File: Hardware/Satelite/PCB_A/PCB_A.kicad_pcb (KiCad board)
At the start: 2 copper layers, 54 x 54 mm, 82 parts, among them J1 Batería LiPo (Soldada), J2 CONUFL001-SMD, J3 Servo Globo, J4 Conector_PCB_A-B, J5 Servo Paracaídas, M1 Spacer, M2 Spacer, M3 Spacer, Q1 SSM3J338R,LF, Q2 BC817, U1 A2235-H, U2 CC1101RGP, U3 0915BM15A0001E, U4 AP9211SA-AF-HAC-7, U5 B39921B3588U410, U6 CC1190, Y1 26 MHz

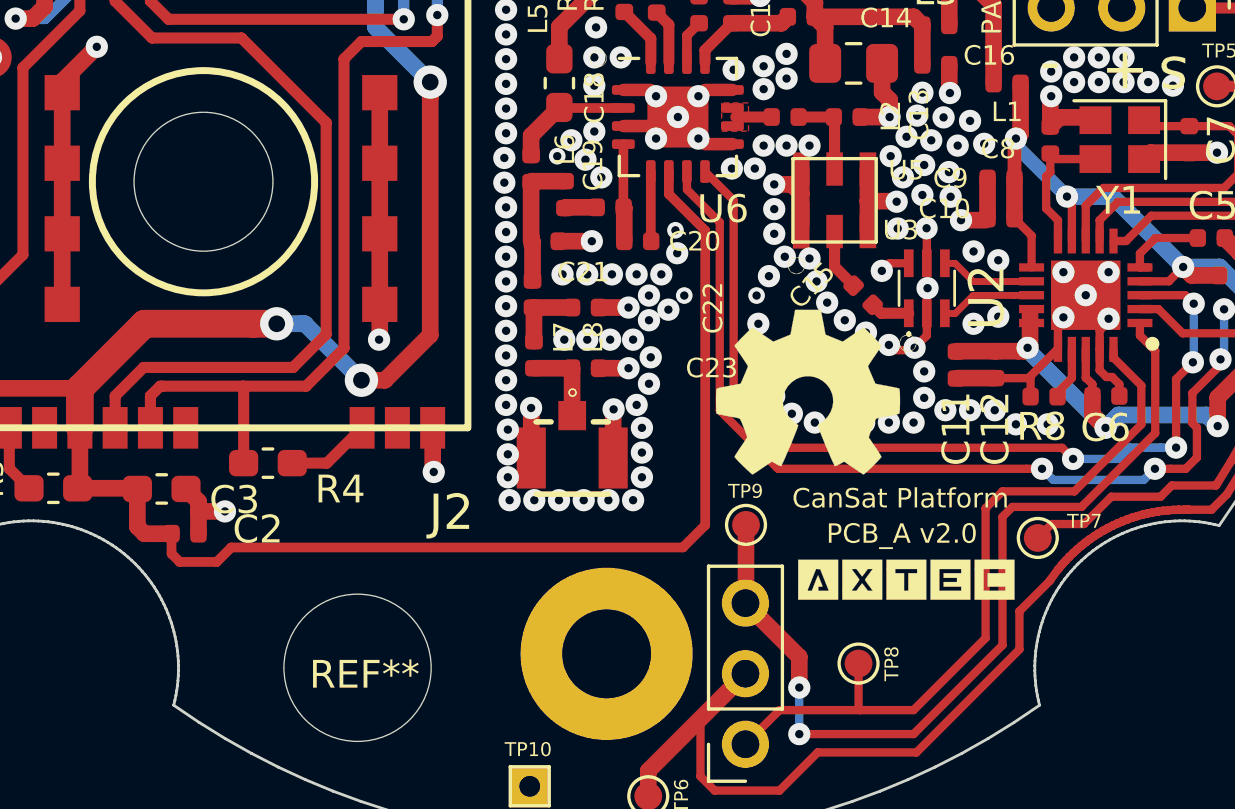
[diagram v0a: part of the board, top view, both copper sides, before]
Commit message: Agregado jumper de seleción de ganacia para CC1190 en ET
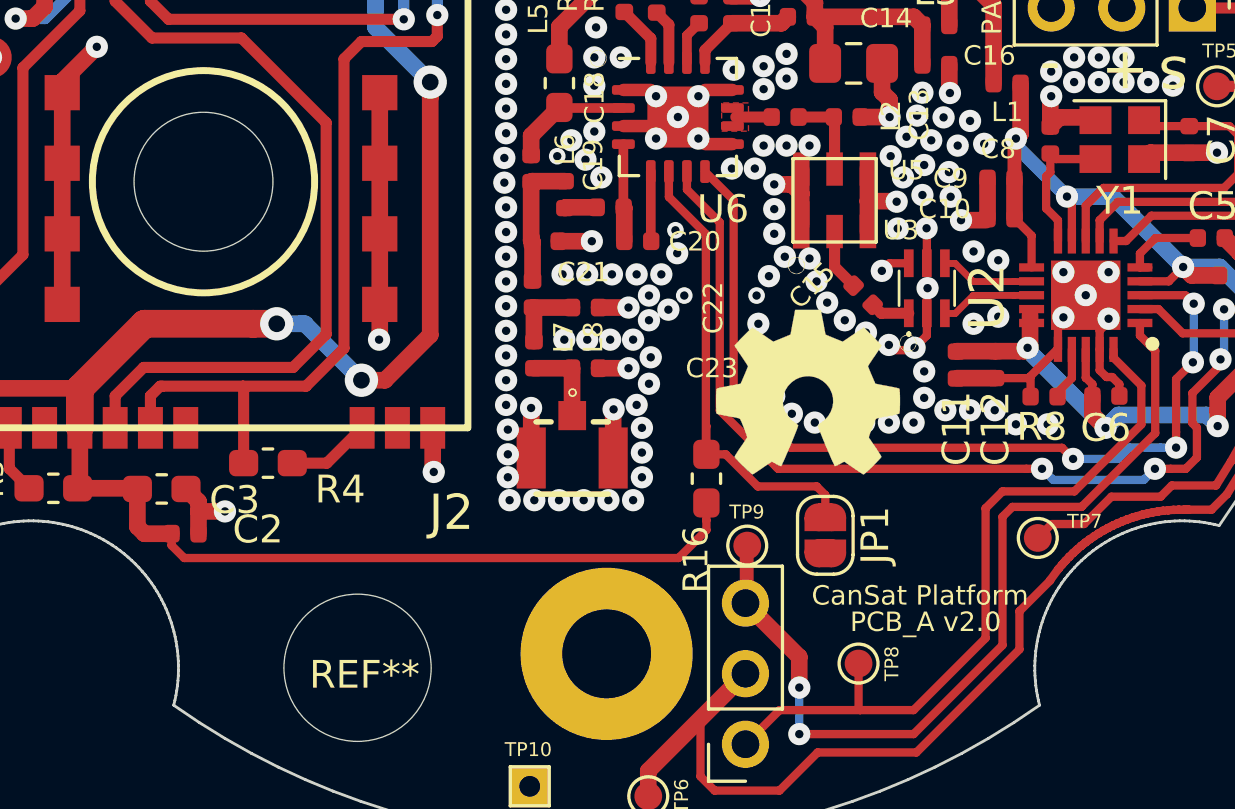
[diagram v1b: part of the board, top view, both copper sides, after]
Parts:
- removed G*** (x2): LOGO, AXTEC:Logo_AXTEC
- added JP1: Jumper, Jumper:SolderJumper-2_P1.3mm_Open_RoundedPad1.0x1.5mm, F.Cu at (7.87, 15.9)
- added R16: 10K, Resistor_SMD:R_0603_1608Metric_Pad1.05x0.95mm_HandSolder, F.Cu at (3.59, 13.9)
- moved TP9 0.75 mm to (5.06, 16.3)
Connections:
- S1 pad 3: Net-(S1-Pad3) -> (no net)
- U1 pad 10: Net-(U1-Pad10) -> (no net)
- U1 pad 11: Net-(U1-Pad11) -> (no net)
- U1 pad 12: Net-(U1-Pad12) -> (no net)
- U1 pad 13: Net-(U1-Pad13) -> (no net)
- U1 pad 14: Net-(U1-Pad14) -> (no net)
- U1 pad 15: Net-(U1-Pad15) -> (no net)
- U1 pad 16: Net-(U1-Pad16) -> (no net)
- U1 pad 2: Net-(U1-Pad2) -> (no net)
- U1 pad 22: Net-(U1-Pad22) -> (no net)
- U1 pad 8: Net-(U1-Pad8) -> (no net)
- U4 pad 4: Net-(U4-Pad4) -> (no net)
- U4 pad 7: Net-(U4-Pad7) -> (no net)
- U6 pad 6: +3V3_Internal -> /CC1101/HGM
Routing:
- net /CC1101/HGM: track 0.00 -> 17.5 mm
- net +3V3_Internal: track 144.5 -> 131.9 mm
- net /SCLK: track 33.5 -> 32.9 mm

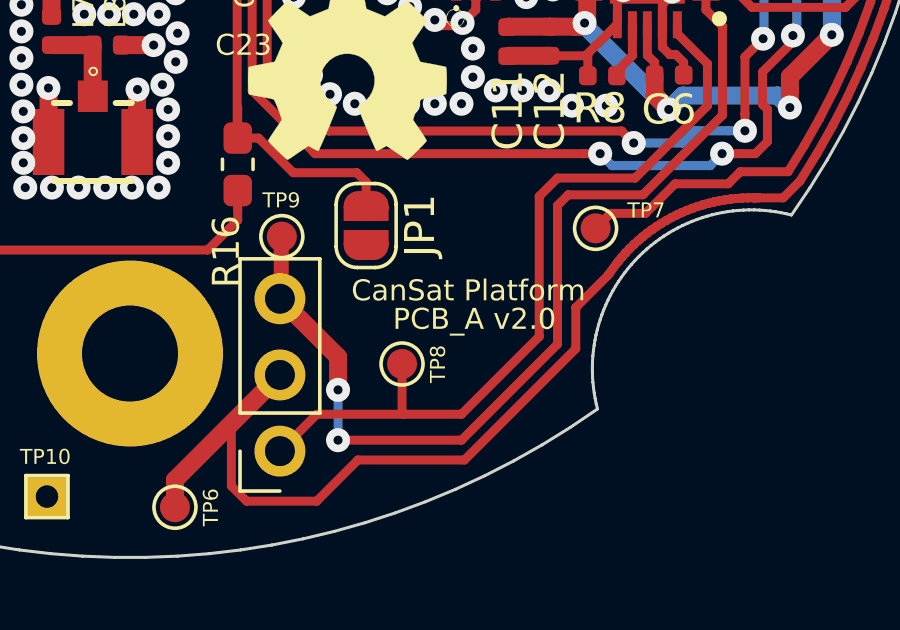
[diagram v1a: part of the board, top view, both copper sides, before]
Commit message: Agregado de logos faltantes en PCB_A
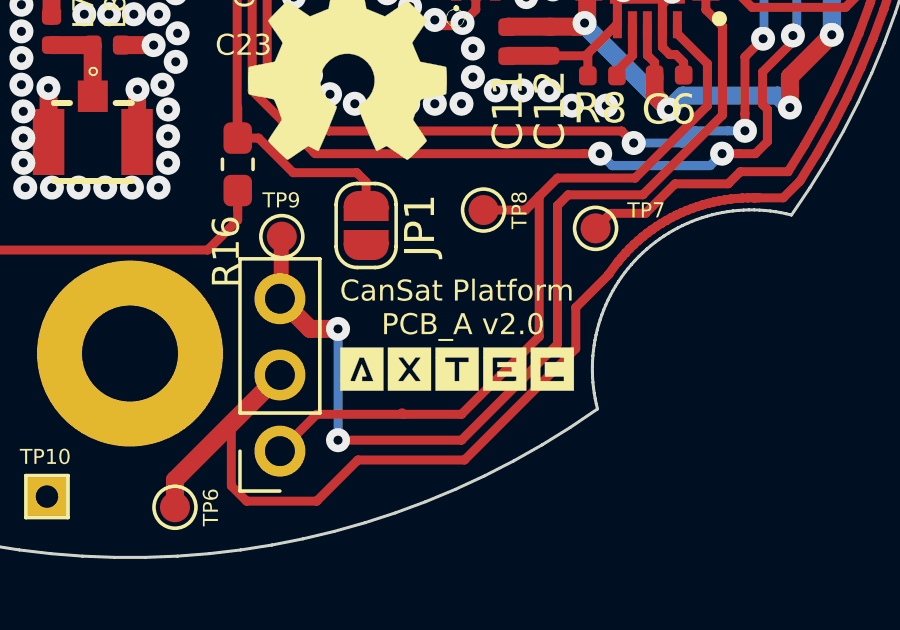
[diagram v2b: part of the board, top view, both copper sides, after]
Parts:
- added G***: LOGO, AXTEC:Logo_AXTEC, B.Cu at (10.8, 20.5)
- added G***: LOGO, AXTEC:Logo_AXTEC, F.Cu at (11.0, 20.5)
- moved TP8 5.81 mm to (11.8, 15.4)
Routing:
- net /SCLK: track 32.9 -> 33.4 mm

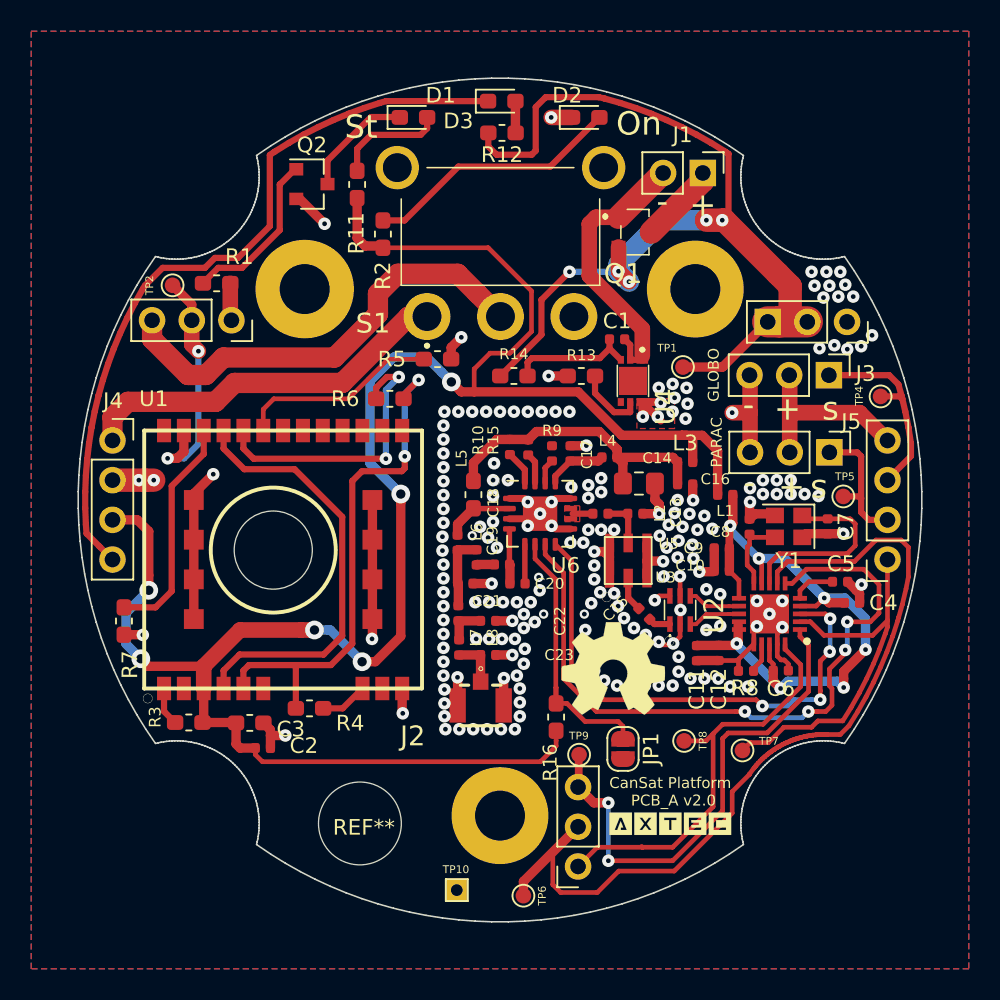
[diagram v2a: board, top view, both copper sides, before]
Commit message: Pequeños arreglos a silkscreen en PCB_A
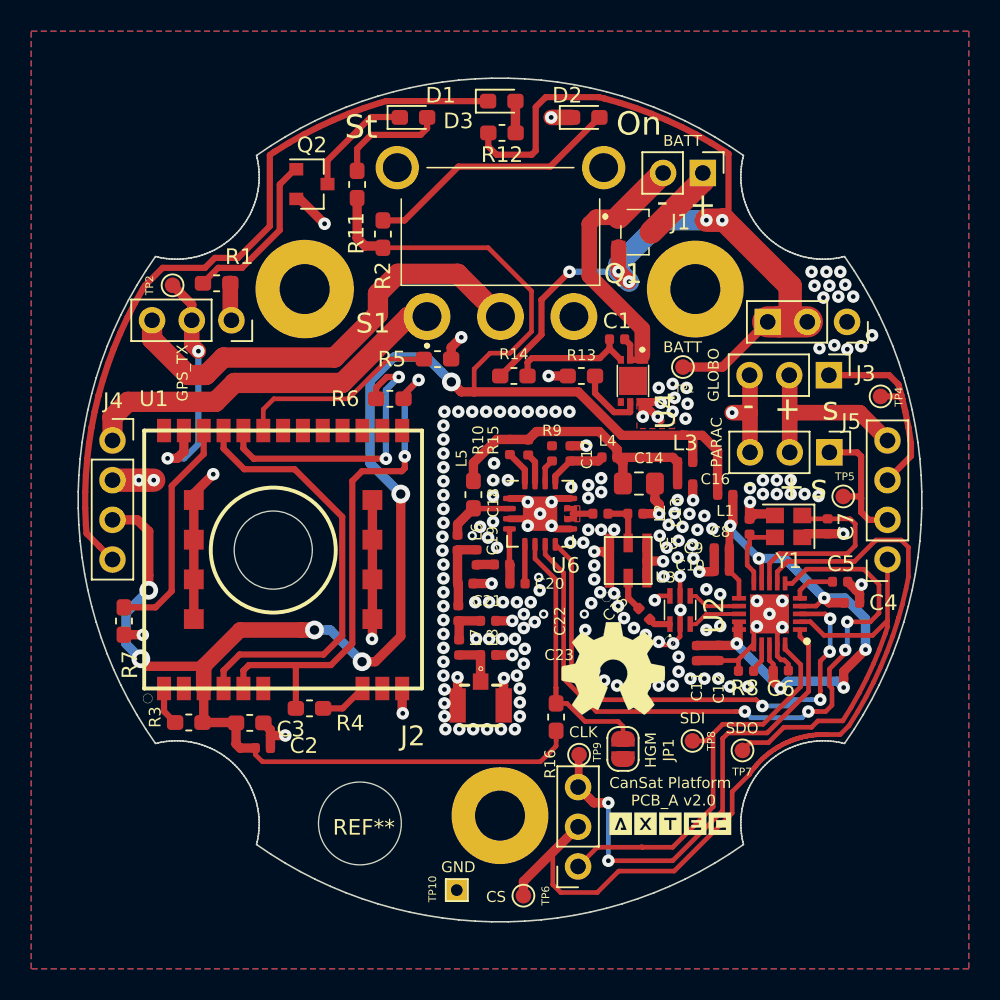
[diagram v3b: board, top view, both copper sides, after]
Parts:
- added ?: , , F.Cu at (9.65, 16.1)
- added ?: , , F.Cu at (10.3, 16.5)
- moved TP8 0.53 mm to (12.3, 15.4)
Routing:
- net /SDI: track 27.0 -> 26.5 mm
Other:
- board text added: "BATT"
- board text added: "CLK"
- board text added: "CS"
- board text added: "GND"
- board text added: "GPS_TX"
- board text added: "HGM"
- board text added: "SDI"
- board text added: "SDO"
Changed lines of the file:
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@@
   (general
     (thickness 1.6)
-    (drawings 39)
-    (tracks 957)
+    (drawings 48)
+    (tracks 958)
     (zones 0)
-    (modules 84)
+    (modules 86)
     (nets 58)
   )
@@
     (add_net /CC1101/RF_P)
   )
+  (module "" (layer F.Cu)
+    (at 9.652 16.129)
+    (fp_text reference "" (at 10.287 16.51) (layer F.SilkS)
+      (effects (font (size 1.27 1.27) (thickness 0.15)))
+    )
+    (fp_text value "" (at 10.287 16.51) (layer F.SilkS)
+      (effects (font (size 1.27 1.27) (thickness 0.15)))
+    )
+  )
+  (module "" (layer F.Cu)
+    (at 10.287 16.51)
+    (fp_text reference "" (at 10.8458 20.5232) (layer F.SilkS)
+      (effects (font (size 1.27 1.27) (thickness 0.15)))
+    )
+    (fp_text value "" (at 10.8458 20.5232) (layer F.SilkS)
+      (effects (font (size 1.27 1.27) (thickness 0.15)))
+    )
+  )
   (module AXTEC:Logo_AXTEC (layer B.Cu)
     (at 10.8458 20.5232 180)
@@
     (tags "resistor handsolder")
     (attr smd)
-    (fp_text reference R16 (at -2.91 -0.38 90) (layer F.SilkS)
-      (effects (font (size 0.9 0.9) (thickness 0.15)))
+    (fp_text reference R16 (at -2.998 -0.38 90) (layer F.SilkS)
+      (effects (font (size 0.7 0.7) (thickness 0.15)))
     )
     (fp_text value 10K (at 0 1.43 90) (layer F.Fab)
@@
     (tags "solder jumper open")
     (attr virtual)
-    (fp_text reference JP1 (at 0 -1.8 270) (layer F.SilkS)
-      (effects (font (size 1 1) (thickness 0.15)))
+    (fp_text reference JP1 (at 0.069 -2.924 90) (layer F.SilkS)
+      (effects (font (size 0.7 0.7) (thickness 0.15)))
     )
     (fp_text value Jumper (at 0 1.9 270) (layer F.Fab)
@@
     (tags "Integrated Circuit")
     (attr smd)
-    (fp_text reference U4 (at -2.0828 -1.651 90) (layer F.SilkS)
+    (fp_text reference U4 (at -2.0828 -1.905 90) (layer F.SilkS)
       (effects (font (size 1.27 1.27) (thickness 0.254)))
     )
@@
     (tags "capacitor handsolder")
     (attr smd)
-    (fp_text reference C14 (at 1.1684 -1.6256) (layer F.SilkS)
+    (fp_text reference C14 (at 0.635 -1.6256) (layer F.SilkS)
       (effects (font (size 0.7 0.7) (thickness 0.15)))
     )
@@
     (descr "Through hole straight pin header, 1x02, 2.54mm pitch, single row")
     (tags "Through hole pin header THT 1x02 2.54mm single row")
-    (fp_text reference J1 (at -2.4384 1.2954) (layer F.SilkS)
+    (fp_text reference J1 (at 3.1496 1.4224) (layer F.SilkS)
       (effects (font (size 1 1) (thickness 0.15)))
     )
@@
     (tags capacitor)
     (attr smd)
-    (fp_text reference C11 (at 2.285 0 270) (layer F.SilkS)
-      (effects (font (size 1 1) (thickness 0.15)))
+    (fp_text reference C11 (at 2.133 0 270) (layer F.SilkS)
+      (effects (font (size 0.7 0.7) (thickness 0.15)))
     )
     (fp_text value 100nF (at 0 1.17 270) (layer F.Fab)
@@
     (attr smd)
     (fp_text reference C12 (at 2.3 0 270) (layer F.SilkS)
-      (effects (font (size 1 1) (thickness 0.15)))
+      (effects (font (size 0.7 0.7) (thickness 0.15)))
     )
     (fp_text value 100nF (at 0 1.17 270) (layer F.Fab)
@@
     (tags "test point SMD pad")
     (attr virtual)
-    (fp_text reference TP1 (at -1.016 -1.2192) (layer F.SilkS)
+    (fp_text reference TP1 (at 0.1016 1.397) (layer F.SilkS)
       (effects (font (size 0.5 0.5) (thickness 0.125)))
     )
@@
     (tags "test point SMD pad")
     (attr virtual)
-    (fp_text reference TP4 (at -1.3716 -0.0381 90) (layer F.SilkS)
+    (fp_text reference TP4 (at 1.1684 0.0254 270) (layer F.SilkS)
       (effects (font (size 0.5 0.5) (thickness 0.125)))
     )
@@
     (tags "test point SMD pad")
     (attr virtual)
-    (fp_text reference TP6 (at 1.2 0 90) (layer F.SilkS)
+    (fp_text reference TP6 (at 1.4224 0 270) (layer F.SilkS)
       (effects (font (size 0.5 0.5) (thickness 0.125)))
     )
@@
     (tags "test point SMD pad")
     (attr virtual)
-    (fp_text reference TP7 (at 1.6891 -0.5969) (layer F.SilkS)
+    (fp_text reference TP7 (at -0.0254 1.3716) (layer F.SilkS)
       (effects (font (size 0.5 0.5) (thickness 0.125)))
     )
@@
   )
   (module TestPoint:TestPoint_Pad_D1.0mm (layer F.Cu)
-    (at 11.7856 15.4178)
+    (at 12.319 15.4178)
     (descr "SMD pad as test Point, diameter 1.0mm")
     (tags "test point SMD pad")
@@
     (tags "test point SMD pad")
     (attr virtual)
-    (fp_text reference TP9 (at -0.0127 -1.2065) (layer F.SilkS)
+    (fp_text reference TP9 (at 1.162 -0.174 90) (layer F.SilkS)
       (effects (font (size 0.5 0.5) (thickness 0.125)))
     )
@@
     (tags "test point THT pad rectangle square")
     (attr virtual)
-    (fp_text reference TP10 (at -0.0508 -1.3208) (layer F.SilkS)
+    (fp_text reference TP10 (at -1.5494 -0.0762 90) (layer F.SilkS)
       (effects (font (size 0.5 0.5) (thickness 0.125)))
     )
@@
     (pad 1 np_thru_hole circle (at 0 0) (size 5.3 5.3) (drill 5.3) (layers *.Cu *.Mask))
   )
+  (gr_text BATT (at 11.684 -22.987) (layer F.SilkS)
+    (effects (font (size 0.7 0.7) (thickness 0.175)))
+  )
+  (gr_text GPS_TX (at -20.32 -8.128 90) (layer F.SilkS)
+    (effects (font (size 0.7 0.7) (thickness 0.175)))
+  )
+  (gr_text CLK (at 5.334 14.859) (layer F.SilkS)
+    (effects (font (size 0.7 0.7) (thickness 0.175)))
+  )
+  (gr_text BATT (at 11.684 -9.779) (layer F.SilkS)
+    (effects (font (size 0.7 0.7) (thickness 0.175)))
+  )
+  (gr_text GND (at -2.667 23.495) (layer F.SilkS)
+    (effects (font (size 0.7 0.7) (thickness 0.175)))
+  )
+  (gr_text CS (at -0.254 25.4) (layer F.SilkS)
+    (effects (font (size 0.7 0.7) (thickness 0.175)))
+  )
+  (gr_text SDI (at 12.319 13.97) (layer F.SilkS)
+    (effects (font (size 0.7 0.7) (thickness 0.175)))
+  )
+  (gr_text SDO (at 15.494 14.605) (layer F.SilkS)
+    (effects (font (size 0.7 0.7) (thickness 0.175)))
+  )
+  (gr_text HGM (at 9.652 16.002 90) (layer F.SilkS)
+    (effects (font (size 0.7 0.7) (thickness 0.175)))
+  )
   (gr_poly (pts (xy 5.0165 -6.223) (xy -3.302 -6.223) (xy -3.302 -5.1435) (xy 5.0165 -5.1435)) (layer F.Mask) (width 0.1))
   (gr_poly (pts (xy 4.8895 5.9055) (xy 6.223 5.9055) (xy 6.223 7.6835) (xy 4.8895 7.6835)) (layer F.Mask) (width 0.1))
@@
   (segment (start 14.2494 14.351) (end 16.8402 14.351) (width 0.3) (layer F.Cu) (net 13))
   (segment (start 16.8402 14.351) (end 19.247788 11.943412) (width 0.3) (layer F.Cu) (net 13))
-  (segment (start 13.1826 15.4178) (end 13.6398 14.9606) (width 0.3) (layer F.Cu) (net 13))
-  (segment (start 11.7856 15.4178) (end 13.1826 15.4178) (width 0.3) (layer F.Cu) (net 13))
+  (segment (start 13.191163 15.409237) (end 13.6398 14.9606) (width 0.3) (layer F.Cu) (net 13))
+  (segment (start 13.1826 15.4178) (end 13.191163 15.409237) (width 0.3) (layer F.Cu) (net 13))
+  (segment (start 12.319 15.4178) (end 13.1826 15.4178) (width 0.3) (layer F.Cu) (net 13))
   (segment (start 4.996841 18.373862) (end 4.996841 19.043041) (width 0.3) (layer F.Cu) (net 14) (status 30))
   (via (at 6.9342 23.0886) (size 0.8) (drill 0.3) (layers F.Cu B.Cu) (net 14))
